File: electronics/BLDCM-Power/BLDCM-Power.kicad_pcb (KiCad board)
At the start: 4 copper layers, 32 x 32 mm, 38 parts, among them J1 501920-3001, J2 53048-0310, J3 53261-0471, J4 53261-0471, J5 FTSH-107-01-L-DV-K, J6 12402012E212A, U1 INA239-Q1, U2 LDL212PV33R, U3 TMC6300-LA, U4 INA239-Q1, U5 TCAN1462, U6 INA239-Q1

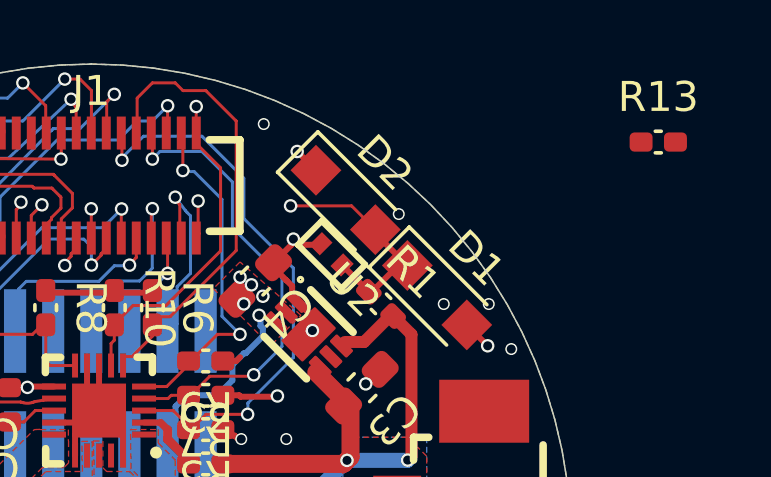
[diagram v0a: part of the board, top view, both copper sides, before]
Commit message: Refactor: Power PCB resistor
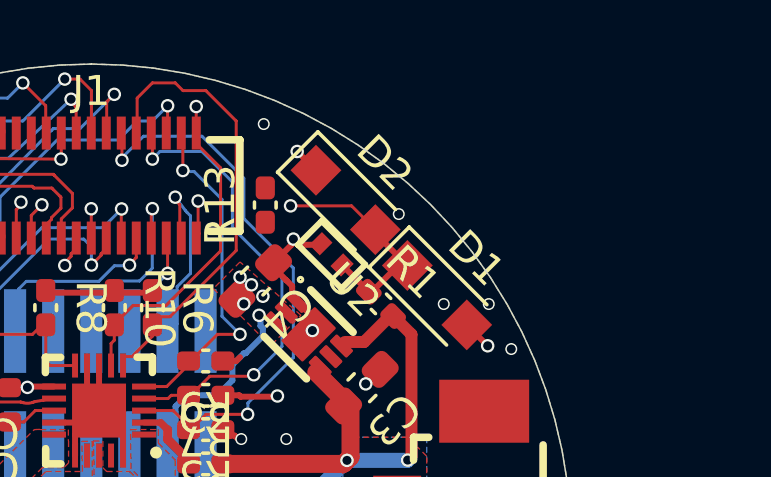
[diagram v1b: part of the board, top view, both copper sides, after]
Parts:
- moved R13 13.3 mm to (154.3, 93.7), turned to 90 degrees
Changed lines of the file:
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@@
 	(footprint "BrenoCQ:R_0402"
 		(layer "F.Cu")
-		(at 167.4011 91.6036)
+		(at 154.3011 93.7036 90)
 		(descr "Resistor")
 		(tags "resistor")
 		(property "Reference" "R13"
-			(at 0 -1.5 0)
+			(at 0 -1.5 90)
 			(unlocked yes)
 			(layer "F.SilkS")
@@
 		)
 		(property "Value" "10K"
-			(at 0 1.5 0)
+			(at 0 1.5 90)
 			(unlocked yes)
 			(layer "F.Fab")
@@
 		)
 		(property "Datasheet" ""
-			(at 0 0 0)
+			(at 0 0 90)
 			(unlocked yes)
 			(layer "F.Fab")
@@
 		)
 		(property "Description" "Resistor"
-			(at 0 0 0)
+			(at 0 0 90)
 			(unlocked yes)
 			(layer "F.Fab")
@@
 		)
 		(fp_line
+			(start 1.11 -0.47)
+			(end 1.11 0.47)
+			(stroke
+				(width 0.05)
+				(type solid)
+			)
+			(layer "F.CrtYd")
+		)
+		(fp_line
 			(start -1.11 -0.47)
 			(end 1.11 -0.47)
+			(stroke
+				(width 0.05)
+				(type solid)
+			)
+			(layer "F.CrtYd")
+		)
+		(fp_line
+			(start 1.11 0.47)
+			(end -1.11 0.47)
 			(stroke
 				(width 0.05)
@@
 		)
 		(fp_line
-			(start 1.11 -0.47)
-			(end 1.11 0.47)
+			(start 0.5 -0.25)
+			(end 0.5 0.25)
 			(stroke
-				(width 0.05)
+				(width 0.1)
 				(type solid)
 			)
-			(layer "F.CrtYd")
-		)
-		(fp_line
-			(start 1.11 0.47)
-			(end -1.11 0.47)
-			(stroke
-				(width 0.05)
-				(type solid)
-			)
-			(layer "F.CrtYd")
+			(layer "F.Fab")
 		)
 		(fp_line
 			(start -0.5 -0.25)
 			(end 0.5 -0.25)
+			(stroke
+				(width 0.1)
+				(type solid)
+			)
+			(layer "F.Fab")
+		)
+		(fp_line
+			(start 0.5 0.25)
+			(end -0.5 0.25)
 			(stroke
 				(width 0.1)
@@
 			(layer "F.Fab")
 		)
-		(fp_line
-			(start 0.5 -0.25)
-			(end 0.5 0.25)
-			(stroke
-				(width 0.1)
-				(type solid)
-			)
-			(layer "F.Fab")
-		)
-		(fp_line
-			(start 0.5 0.25)
-			(end -0.5 0.25)
-			(stroke
-				(width 0.1)
-				(type solid)
-			)
-			(layer "F.Fab")
-		)
 		(fp_text user "${REFERENCE}"
-			(at 0 3 0)
+			(at 0 3 90)
 			(unlocked yes)
 			(layer "F.Fab")
@@
 		)
 		(pad "1" smd roundrect
-			(at -0.5725 0)
+			(at -0.5725 0 90)
 			(size 0.765 0.64)
 			(layers "F.Cu" "F.Mask" "F.Paste")
@@
 		)
 		(pad "2" smd roundrect
-			(at 0.5725 0)
+			(at 0.5725 0 90)
 			(size 0.765 0.64)
 			(layers "F.Cu" "F.Mask" "F.Paste")

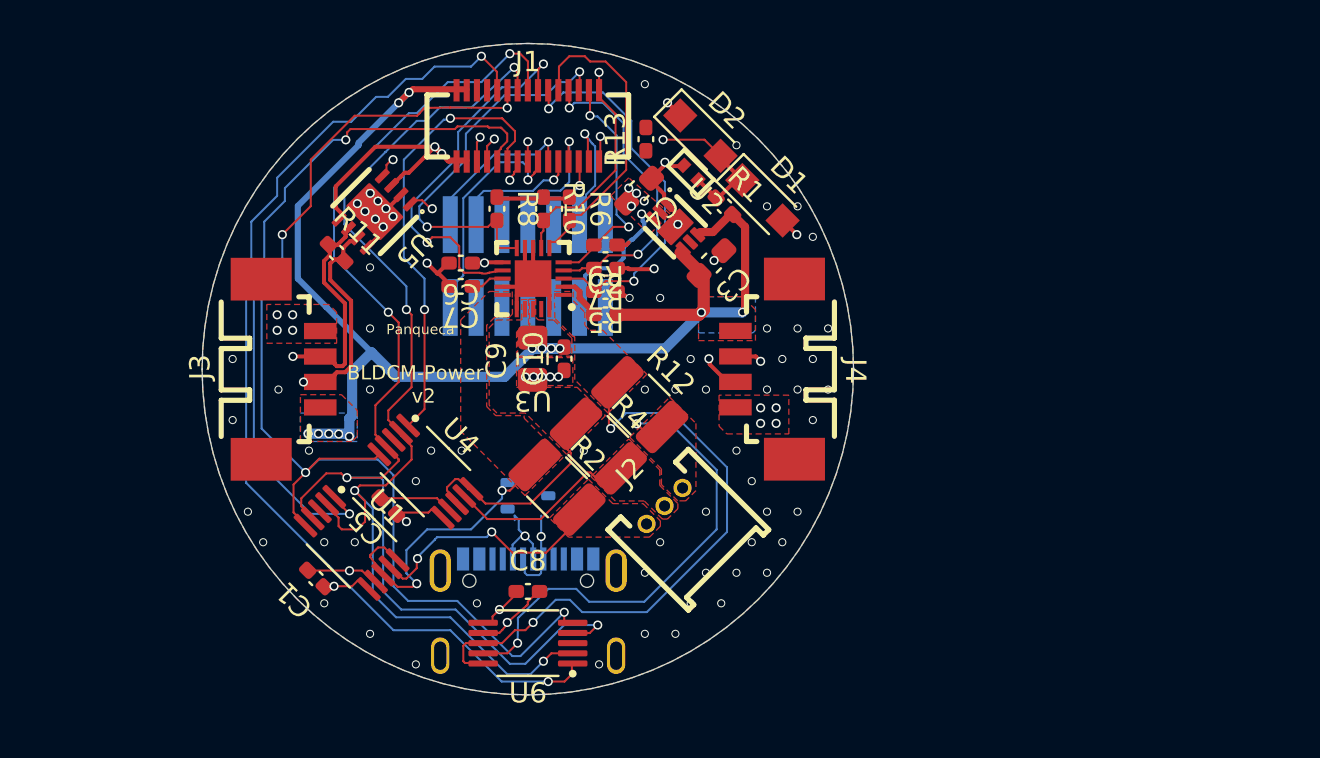
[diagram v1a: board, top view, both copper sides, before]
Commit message: Feat: Power PCB replace symbols with brenocq lib symbols
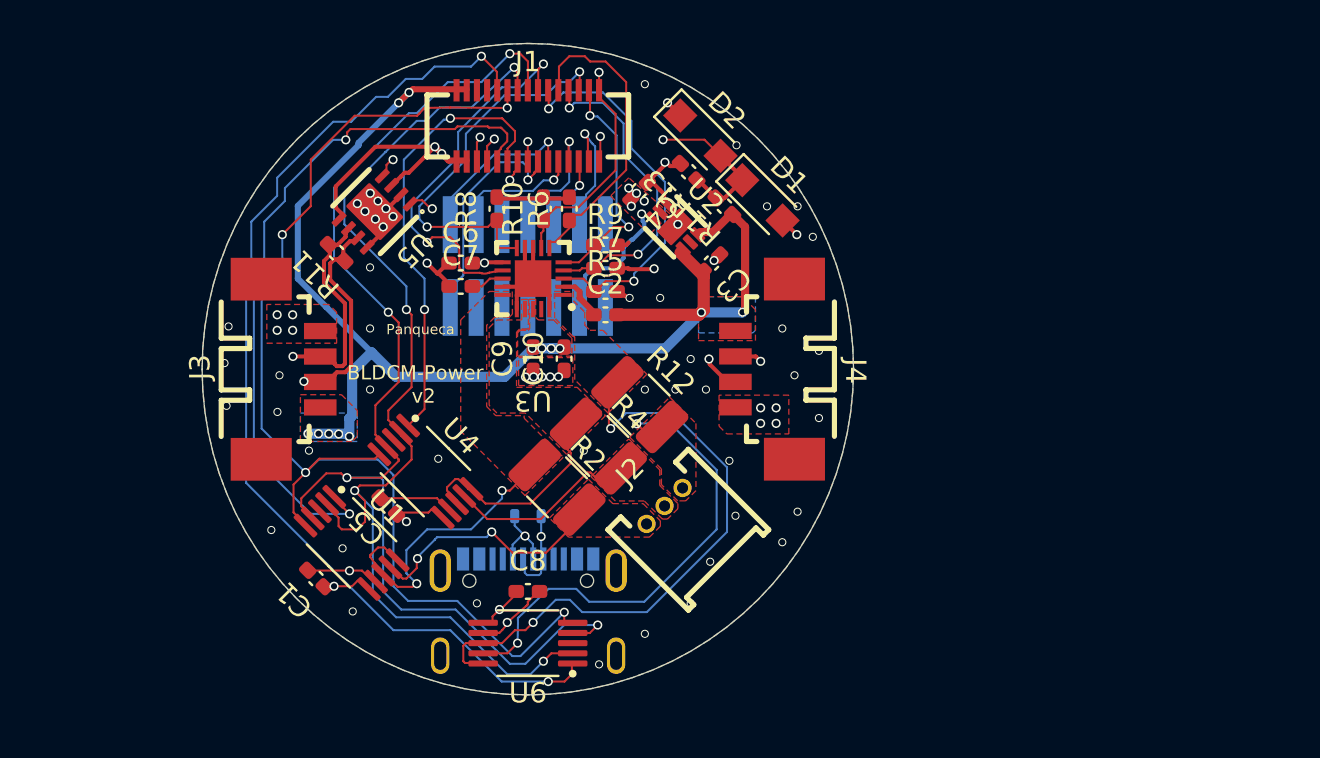
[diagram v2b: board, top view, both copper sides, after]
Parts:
- removed R3: 10K, brenocqLib:RES_0402
- C3, C4: footprint BrenoCQ:C_0603 -> BrenoCQ:C_0402
- C9: footprint BrenoCQ:C_0805 -> BrenoCQ:C_0402
- moved R13 2.64 mm to (156.4, 95.3), turned to 135 degrees
- turned C6 to 0 degrees
- turned C7 to 0 degrees
- turned D3 to 90 degrees
- turned R1 to 135 degrees
- turned R10 to 90 degrees
- turned R11 to 135 degrees
- turned R5 to 0 degrees
- turned R6 to 90 degrees
- turned R7 to 0 degrees
- turned R8 to 90 degrees
- turned R9 to 0 degrees
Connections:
- C1 pad 1: GND -> 3.3V
- C1 pad 2: 3.3V -> GND
- C10 pad 1: VIN -> GND
- C10 pad 2: GND -> VIN
- C2 pad 1: VIN -> Net-(U3-VCP)
- C2 pad 2: Net-(U3-VCP) -> VIN
- C3 pad 1: VIN -> GND
- C3 pad 2: GND -> VIN
- C4 pad 1: 3.3V -> GND
- C4 pad 2: GND -> 3.3V
- C5 pad 1: GND -> 3.3V
- C5 pad 2: 3.3V -> GND
- C6 pad 1: 3.3V -> GND
- C6 pad 2: GND -> 3.3V
- C7 pad 1: Net-(U3-1.8VOUT) -> GND
- C7 pad 2: GND -> Net-(U3-1.8VOUT)
- C8 pad 1: GND -> 3.3V
- C8 pad 2: 3.3V -> GND
- C9 pad 1: VIN -> GND
- C9 pad 2: GND -> VIN
- U2 pad 5: (no net) -> unconnected-(U2-NC-Pad5)
- U3 pad 19: (no net) -> unconnected-(U3---Pad19)
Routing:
- net CAN_N: track 38.4 -> 0.00 mm, vias 2 -> 0
- net /CAN_N: track 0.00 -> 38.4 mm, vias 0 -> 2
- net CAN_P: track 36.5 -> 0.00 mm, vias 2 -> 0
- net /CAN_P: track 0.00 -> 36.5 mm, vias 0 -> 2
- net TMC.VL: track 19.3 -> 0.00 mm, vias 2 -> 0
- net /TMC.VL: track 0.00 -> 19.3 mm, vias 0 -> 2
- net TMC.UH: track 19.1 -> 0.00 mm, vias 2 -> 0
- net /TMC.UH: track 0.83 -> 19.1 mm, vias 1 -> 2
- net TMC.VH: track 15.6 -> 0.00 mm, vias 2 -> 0
- net TMC.UL: track 15.3 -> 0.00 mm
- net /TMC.UL: track 0.00 -> 15.3 mm
- net TCM.U.IN: track 14.9 -> 0.00 mm, vias 2 -> 0
- net /TCM.U.IN: track 0.00 -> 14.9 mm, vias 0 -> 2
- net /TMC.VH: track 1.95 -> 15.6 mm, vias 1 -> 2
- net /VOLT: track 0.00 -> 12.1 mm, vias 0 -> 2
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
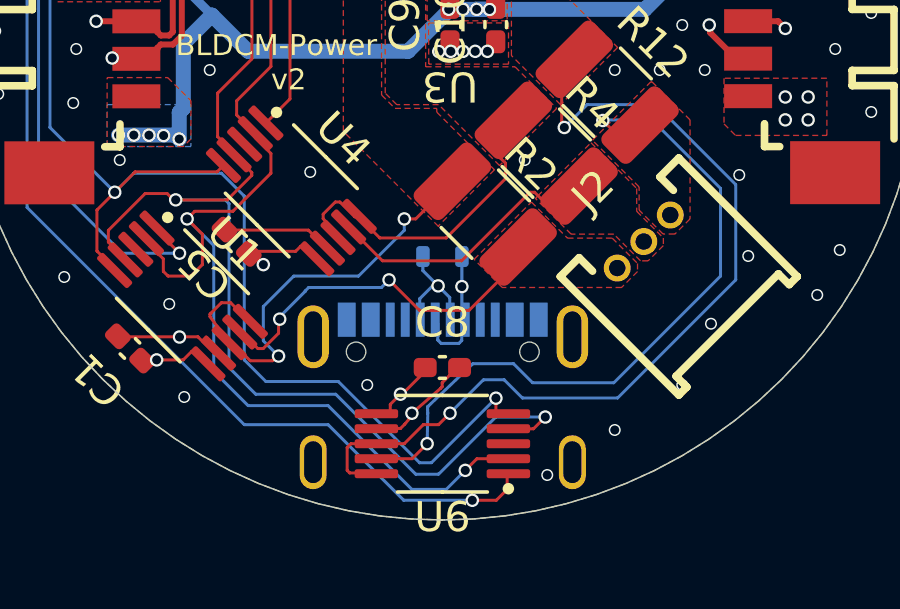
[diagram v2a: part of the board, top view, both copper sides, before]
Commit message: Feat(pcb): Create net classes in power PCB
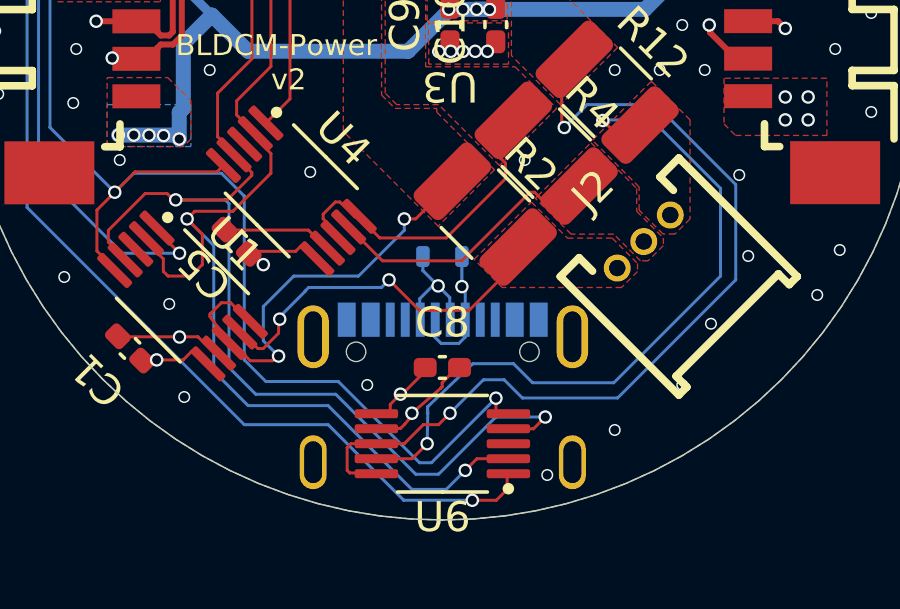
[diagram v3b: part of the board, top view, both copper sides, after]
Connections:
- net /CAN_N renamed /CAN.DN
- net /CAN_P renamed /CAN.DP
- net /TCM.DIAG renamed /TMC.DIAG
- net /TCM.U.IN renamed /TMC.U.IN
- net /TCM.U.OUT renamed /TMC.U.OUT
- net /TCM.V.IN renamed /TMC.V.IN
- net /TCM.V.OUT renamed /TMC.V.OUT
- net /TCM.W.IN renamed /TMC.W.IN
- net /TCM.W.OUT renamed /TMC.W.OUT
- net /USB_N renamed /USB.DN
- net /USB_P renamed /USB.DP

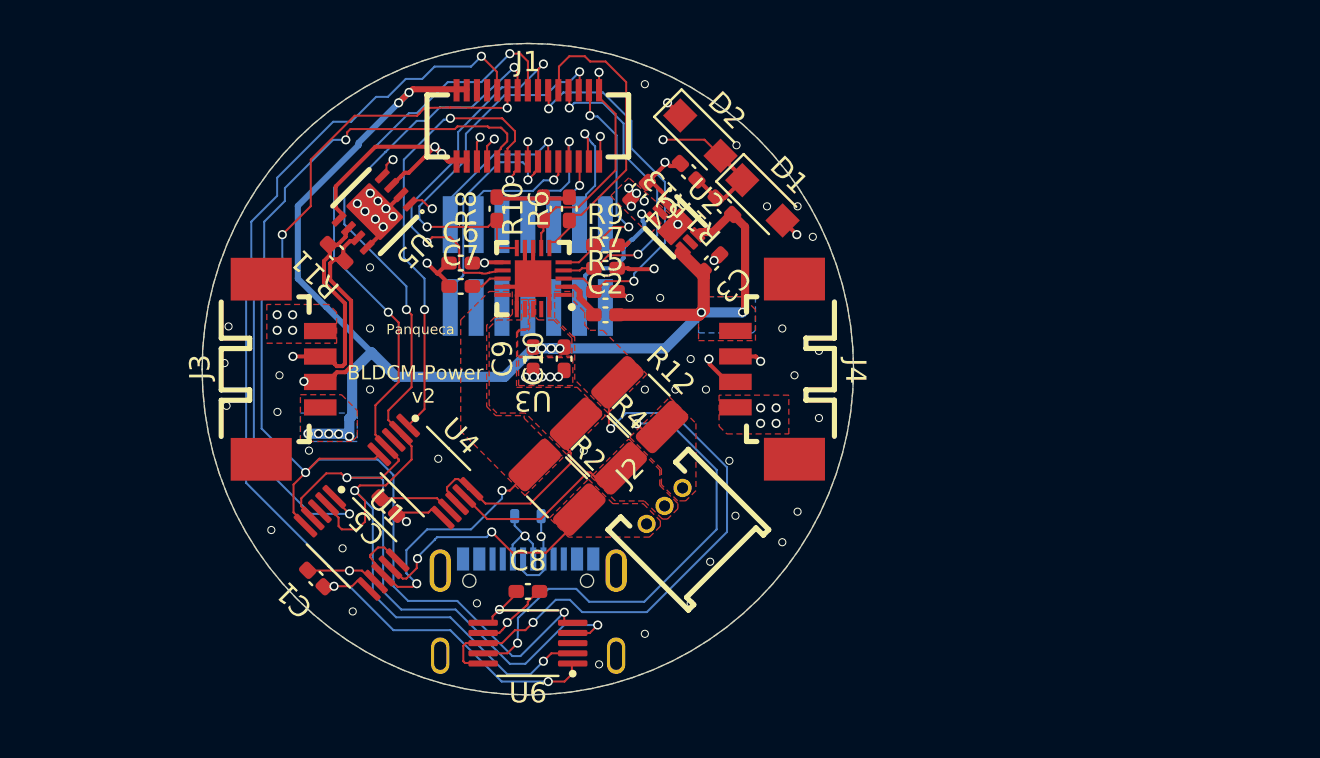
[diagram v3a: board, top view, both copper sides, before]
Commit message: Feat(pcb): Route differential pairs in Power PCB
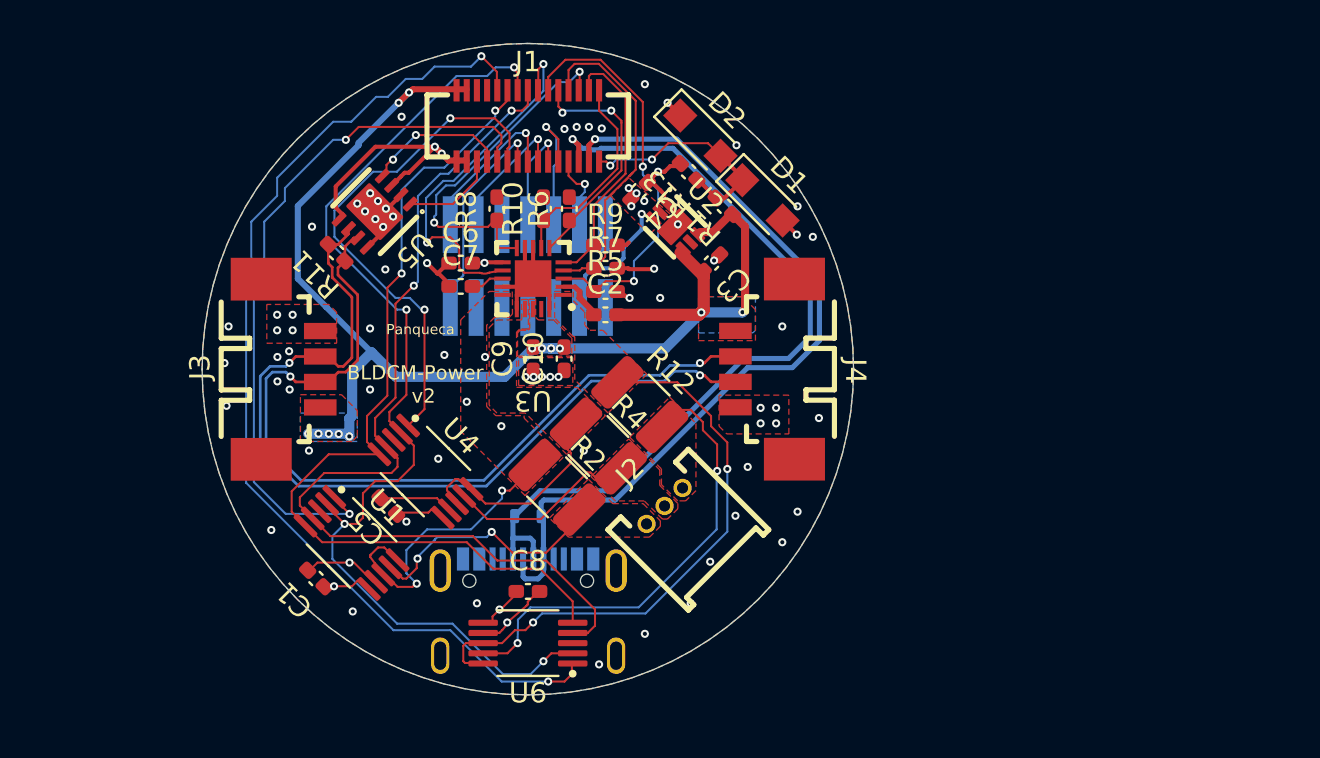
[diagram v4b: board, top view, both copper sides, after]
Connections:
- J1 pad 13: /CAN.TX -> /VCP.RX
- J1 pad 15: /CAN.RX -> /VCP.TX
- J1 pad 17: /VCP.RX -> /RST
- J1 pad 19: /VCP.TX -> /SWO
- J1 pad 21: /RST -> /SWCLK
- J1 pad 23: /SWO -> /SWDIO
- J1 pad 25: /SWCLK -> /USB.DP
- J1 pad 27: /SWDIO -> /USB.DN
- J1 pad 5: /USB.DP -> /CAN.TX
- J1 pad 7: /USB.DN -> /CAN.RX
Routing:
- net /USB.DP: track 25.9 -> 40.6 mm, vias 2 -> 1
- net /INA.CLK: track 57.9 -> 43.9 mm, vias 4 -> 2
- net /USB.DN: track 26.7 -> 40.7 mm, vias 2 -> 1
- net /INA.POCI: track 57.9 -> 47.1 mm, vias 4 -> 2
- net /CAN.DP: track 36.5 -> 41.4 mm
- net GND: track 40.1 -> 35.7 mm, vias 67 -> 71
- net /CAN.DN: track 38.4 -> 42.6 mm
- net /INA.CS1: track 22.0 -> 25.4 mm
- net /TMC.UL: track 15.3 -> 12.2 mm, vias 0 -> 2
- net /SWCLK: track 3.95 -> 7.01 mm
- net /CAN.RX: track 9.69 -> 7.10 mm
- net /SWDIO: track 6.17 -> 3.77 mm
- net /CAN.TX: track 7.21 -> 4.91 mm, vias 2 -> 0
- net /TMC.W.IN: track 30.3 -> 28.4 mm
- net /TMC.VL: track 19.3 -> 17.4 mm
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
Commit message: Feat(pcb): Fix DRC for Power PCB
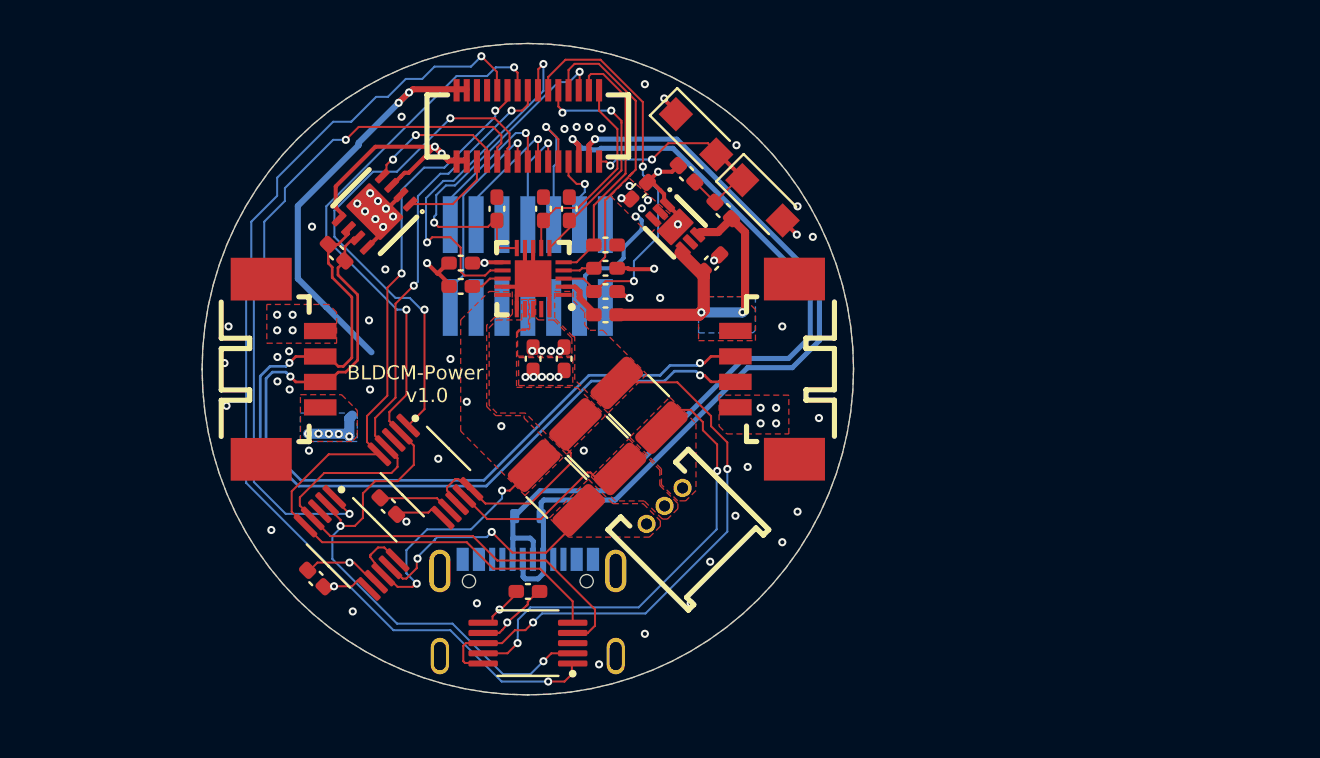
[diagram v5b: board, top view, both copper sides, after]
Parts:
- moved D2 0.22 mm to (156.8, 93.5)
- moved R1 0.21 mm to (158.1, 97.2)
- moved R13 0.14 mm to (156.3, 95.4)
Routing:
- net VIN: track 63.3 -> 61.4 mm
- net GND: track 35.7 -> 35.1 mm, vias 71 -> 70
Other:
- rule pad_to_mask_clearance: 0.075 -> 0.05
- board text added: "v1.0"
- board text removed: "Panqueca"
- board text removed: "v2"
